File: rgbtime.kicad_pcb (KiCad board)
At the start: 2 copper layers, 50 x 50 mm, 4 parts

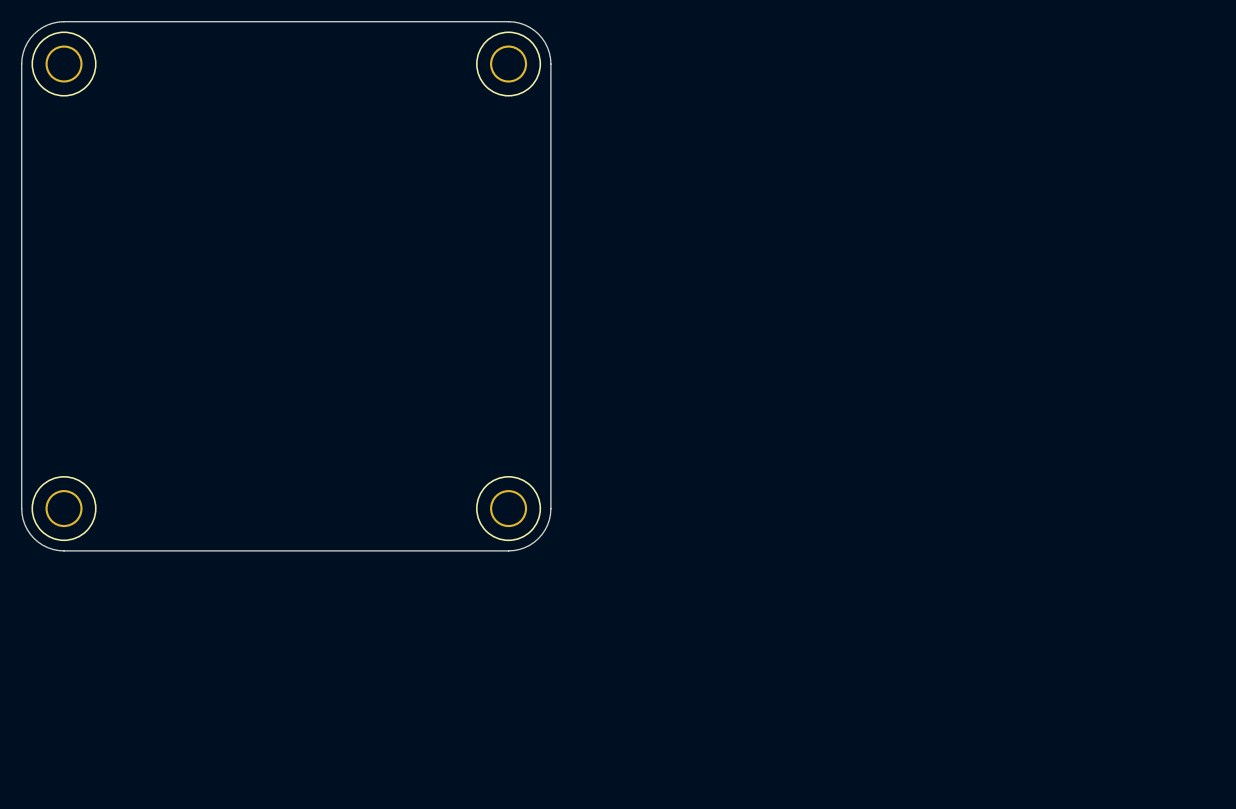
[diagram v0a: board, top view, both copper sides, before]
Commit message: started layout, matrix placed, need USB footprint
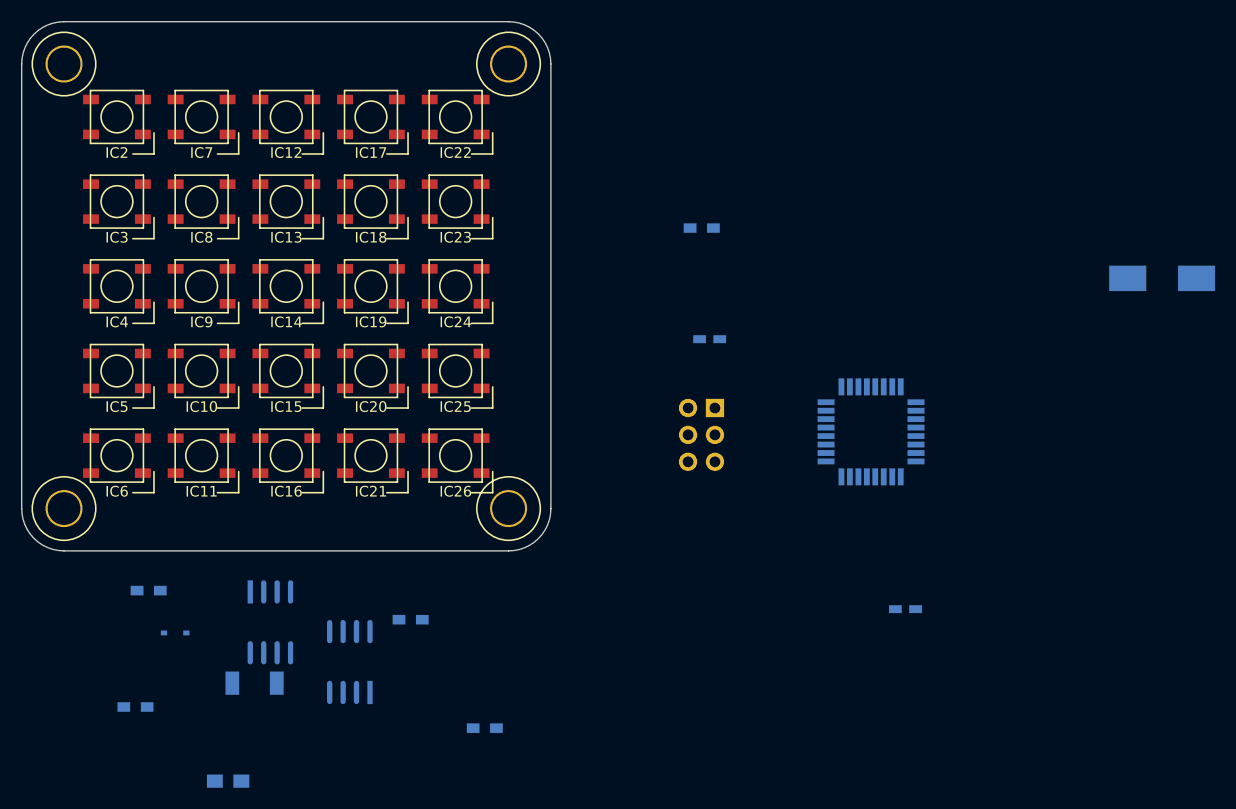
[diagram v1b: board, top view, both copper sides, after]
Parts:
- added C1: 0.1u, Capacitors_SMD:C_0603_HandSoldering, B.Cu at (214.5, 134.5)
- added C2: 0.1u, Capacitors_SMD:C_0603_HandSoldering, B.Cu at (196.0, 109.0)
- added C3: SMD GC 0,22/5,5, Capacitors_SMD:c_elec_8x10.5, B.Cu at (238.8, 103.2)
- added C4: 1u, Capacitors_SMD:C_0805_HandSoldering, B.Cu at (150.5, 150.8)
- added CON1: AVR-ISP-6, Pin_Headers:Pin_Header_Straight_2x03, B.Cu at (196.5, 115.5)
- added D1: 1N4148WS, Diodes_SMD:SOD-323, B.Cu at (145.5, 136.8)
- added IC1: ATMEGA8-AI, Housings_QFP:TQFP-32_7x7mm_Pitch0.8mm, B.Cu at (211.2, 117.8)
- added IC10: WS2812B, devthrash:WS2812B, F.Cu at (148.0, 112.0)
- added IC11: WS2812B, devthrash:WS2812B, F.Cu at (148.0, 120.0)
- added IC12: WS2812B, devthrash:WS2812B, F.Cu at (156.0, 88.0)
- added IC13: WS2812B, devthrash:WS2812B, F.Cu at (156.0, 96.0)
- added IC14: WS2812B, devthrash:WS2812B, F.Cu at (156.0, 104.0)
- added IC15: WS2812B, devthrash:WS2812B, F.Cu at (156.0, 112.0)
- added IC16: WS2812B, devthrash:WS2812B, F.Cu at (156.0, 120.0)
- added IC17: WS2812B, devthrash:WS2812B, F.Cu at (164.0, 88.0)
- added IC18: WS2812B, devthrash:WS2812B, F.Cu at (164.0, 96.0)
- added IC19: WS2812B, devthrash:WS2812B, F.Cu at (164.0, 104.0)
- added IC2: WS2812B, devthrash:WS2812B, F.Cu at (140.0, 88.0)
- added IC20: WS2812B, devthrash:WS2812B, F.Cu at (164.0, 112.0)
- added IC21: WS2812B, devthrash:WS2812B, F.Cu at (164.0, 120.0)
- added IC22: WS2812B, devthrash:WS2812B, F.Cu at (172.0, 88.0)
- added IC23: WS2812B, devthrash:WS2812B, F.Cu at (172.0, 96.0)
- added IC24: WS2812B, devthrash:WS2812B, F.Cu at (172.0, 104.0)
- added IC25: WS2812B, devthrash:WS2812B, F.Cu at (172.0, 112.0)
- added IC26: WS2812B, devthrash:WS2812B, F.Cu at (172.0, 120.0)
- added IC3: WS2812B, devthrash:WS2812B, F.Cu at (140.0, 96.0)
- added IC4: WS2812B, devthrash:WS2812B, F.Cu at (140.0, 104.0)
- added IC5: WS2812B, devthrash:WS2812B, F.Cu at (140.0, 112.0)
- added IC6: WS2812B, devthrash:WS2812B, F.Cu at (140.0, 120.0)
- added IC7: WS2812B, devthrash:WS2812B, F.Cu at (148.0, 88.0)
- added IC8: WS2812B, devthrash:WS2812B, F.Cu at (148.0, 96.0)
- added IC9: WS2812B, devthrash:WS2812B, F.Cu at (148.0, 104.0)
- added R1: 10k, Resistors_SMD:R_0603_HandSoldering, B.Cu at (174.8, 145.8)
- added R2: 150, Resistors_SMD:R_0603_HandSoldering, B.Cu at (167.8, 135.5)
- added R3: 10k, Resistors_SMD:R_0603_HandSoldering, B.Cu at (141.8, 143.8)
- added R4: 10k, Resistors_SMD:R_0603_HandSoldering, B.Cu at (143.0, 132.8)
- added R5: 10, Resistors_SMD:R_0603_HandSoldering, B.Cu at (195.2, 98.5)
- added U1: MCP79410, devthrash:SO8, B.Cu at (162.0, 139.5)
- added U2: LM75, devthrash:SO8, B.Cu at (154.5, 135.8)
- added Y1: CC4V-T1A-32768, devthrash:CC4V-T1A, B.Cu at (153.0, 141.5)
